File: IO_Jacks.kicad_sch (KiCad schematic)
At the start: 45 parts, among them J10 3085_MiniJack_Thonk_Vert, J11 3085_MiniJack_Thonk_Vert, J12 3085_MiniJack_Thonk_Vert, J13 3085_MiniJack_Thonk_Vert, J5 CV_OFFSET, J6 3085_MiniJack_Thonk_Vert, J7 3085_MiniJack_Thonk_Vert, J8 3085_MiniJack_Thonk_Vert, J9 3085_MiniJack_Thonk_Vert, U5 4014_Voltage_Reference_5V_SOT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

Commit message: some more routing
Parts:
- removed TP21: DAC_VOUT0, Shulltronics_Generics:TestPoint_Pad_D2.0mm, symbol Shulltronics_Sch_Symbols:TestPoint
- removed TP25: DAC_VOUT2, Shulltronics_Generics:TestPoint_Pad_D2.0mm, symbol Shulltronics_Sch_Symbols:TestPoint
- removed TP26: DAC_VOUT3, Shulltronics_Generics:TestPoint_Pad_D2.0mm, symbol Shulltronics_Sch_Symbols:TestPoint
- removed TP29: TRIG1, Shulltronics_Generics:TestPoint_Pad_D2.0mm, symbol Shulltronics_Sch_Symbols:TestPoint
- removed TP30: TRIG2, Shulltronics_Generics:TestPoint_Pad_D2.0mm, symbol Shulltronics_Sch_Symbols:TestPoint
- removed TP31: TRIG3, Shulltronics_Generics:TestPoint_Pad_D2.0mm, symbol Shulltronics_Sch_Symbols:TestPoint
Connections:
- net TRIG2: now also U8.12 (4IN+); no longer U8.10 (3IN+)
- net TRIG2_FB: now also U8.13 (4IN-), U8.14 (4OUT); no longer U8.8 (3OUT), U8.9 (3IN-)
- net TRIG3: now also U8.10 (3IN+); no longer U8.12 (4IN+)
- net TRIG3_FB: now also U8.8 (3OUT), U8.9 (3IN-); no longer U8.13 (4IN-), U8.14 (4OUT)
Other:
- moved on the sheet: U8C, U8D

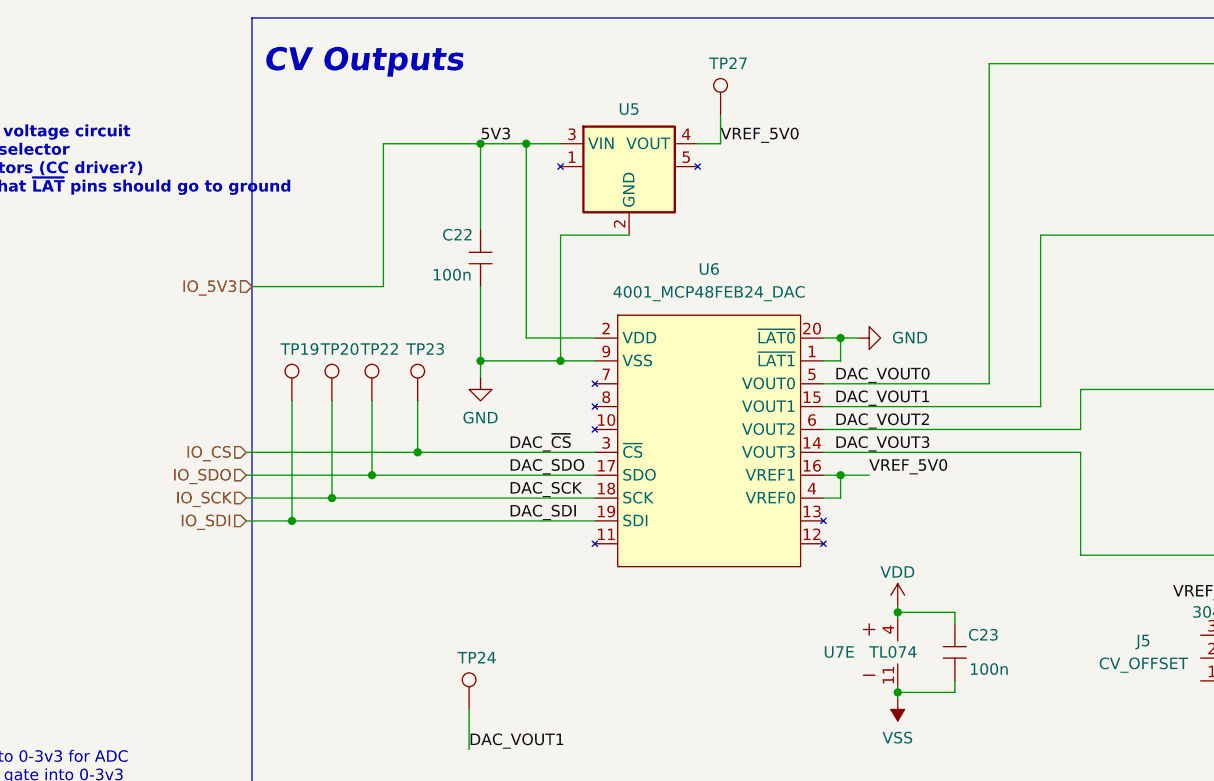
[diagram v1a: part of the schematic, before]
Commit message: Added a few 0 ohm options, finished routing, ordered board!
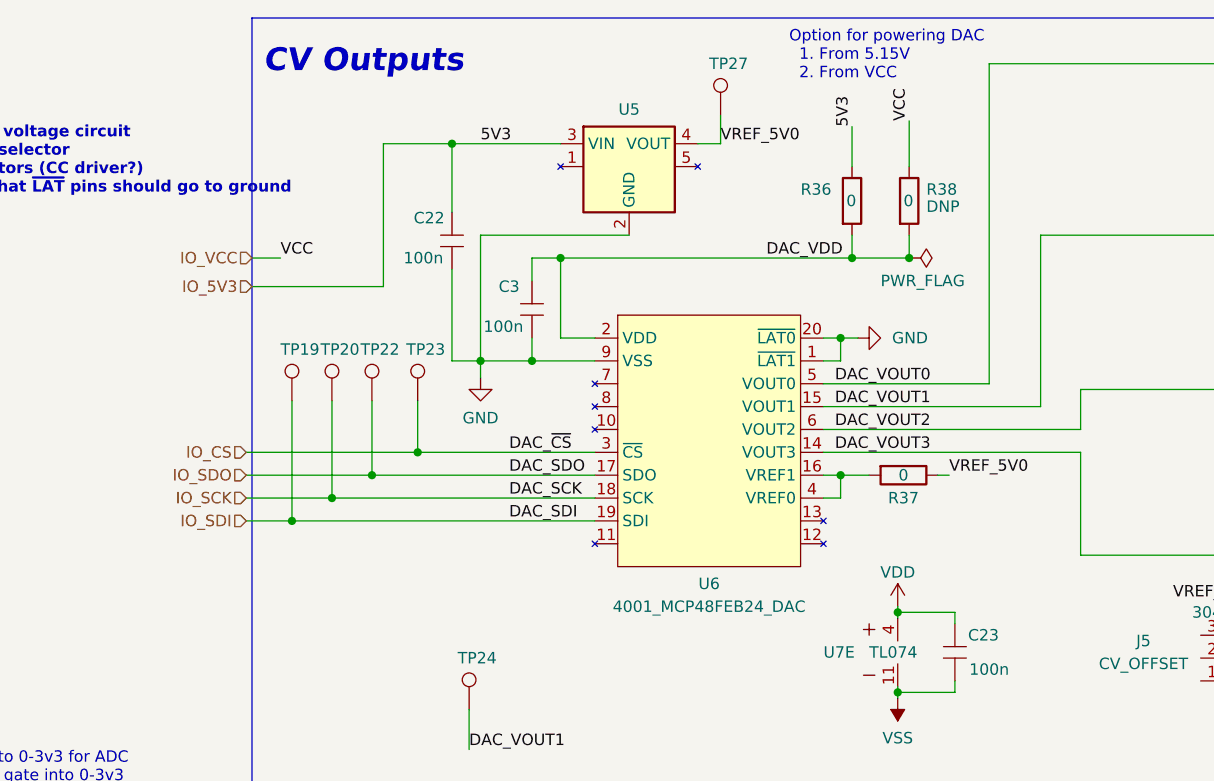
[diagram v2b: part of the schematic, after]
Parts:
- added C3: 3089_Capacitor_100n_16V_SMD, Shulltronics_Generics:C_0402_HandSolder, symbol Shulltronics_Passives:3089_Capacitor_100n_16V_0402
- added R36: 4021_Resistor_SMD_Jumper, Shulltronics_Generics:RES-0402, symbol Shulltronics_Passives:4021_Resistor_SMD_Jumper
- added R37: JMP, Shulltronics_Generics:RES-0402, symbol Shulltronics_Passives:4021_Resistor_SMD_Jumper
- added R38: DNP, Shulltronics_Generics:RES-0402, symbol Shulltronics_Passives:4021_Resistor_SMD_Jumper
- J5: footprint Shulltronics_Connectors:3046_Header_3pos_2.54mm -> Shulltronics_Generics:SMD_SolderJumper-3
- TP19: value DAC_SDI -> SDI
- TP20: value DAC_SCK -> SCK
- TP22: value DAC_SDO -> SDO
- TP23: value DAC_~{CS} -> ~{CS}
- TP24: value DAC_VOUT1 -> DAC1
- TP27: value VREF_5V0 -> 5V0
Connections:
- net GND: now also C3.1
- net IO_5V3: now also R36.1; no longer U6.2 (VDD)
- net VREF_5V0: now also R37.1; no longer U6.16 (VREF1), U6.4 (VREF0)
- new net: R37.2, U6.16 (VREF1), U6.4 (VREF0)
- new net DAC_VDD: C3.2, R36.2, R38.2, U6.2 (VDD)
- new net IO_VCC: R38.1
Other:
- note added: "Option for powering DAC 1. From 5.15V 2. From VCC"
- moved on the sheet: C22

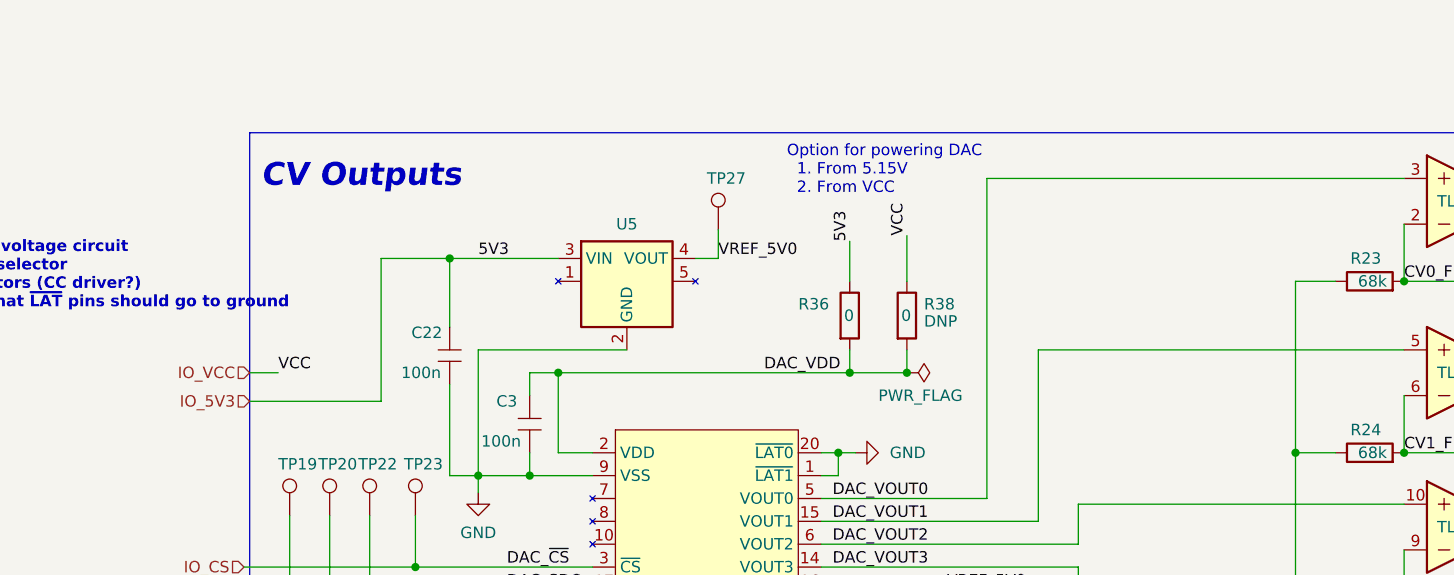
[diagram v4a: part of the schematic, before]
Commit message: Updated a few things from testing voltage regulators
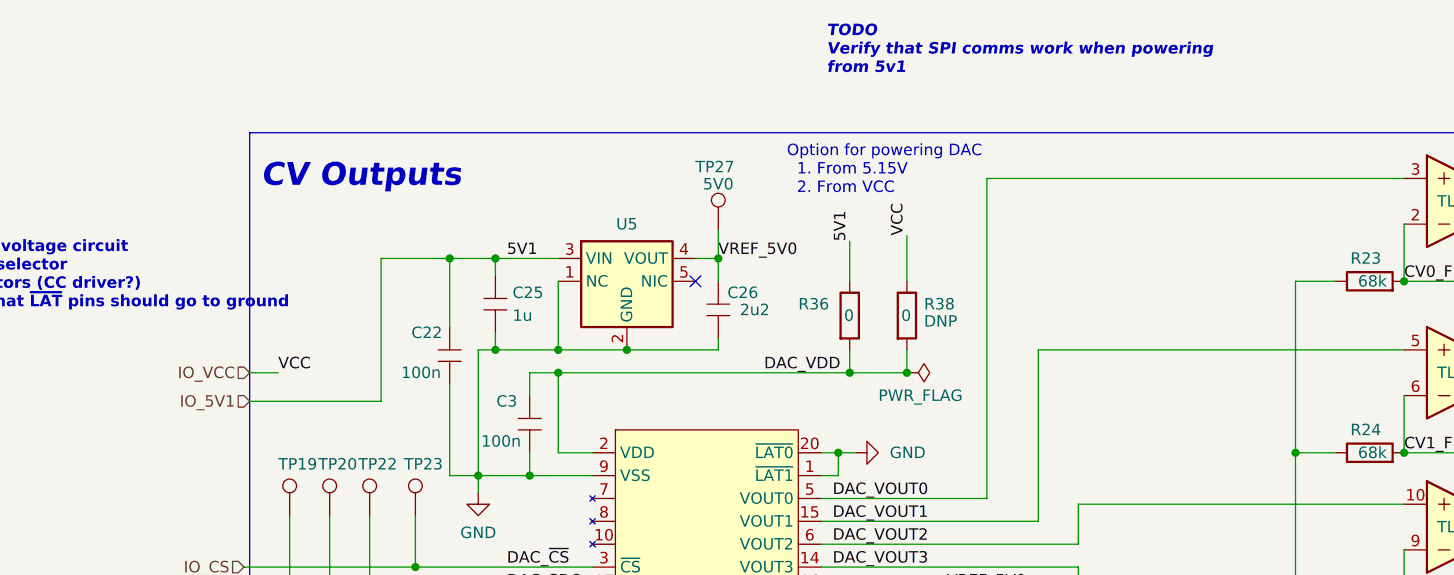
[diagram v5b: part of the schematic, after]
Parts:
- added C25: 4013_Capacitor_1u_16V_0402, Shulltronics_Generics:C_0402_HandSolder, symbol Shulltronics_Passives:4013_Capacitor_1u_16V_0402
- added C26: 4035_Capacitor_2u2_25V_0402, Shulltronics_Generics:C_0402_HandSolder, symbol Shulltronics_Passives:4035_Capacitor_2u2_25V_0402
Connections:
- net GND: now also U5.1 (NC), C25.1, C26.2
- net VREF_5V0: now also C26.1
- net IO_5V3 renamed IO_5V1
- net IO_5V1: now also C25.2
- no-connect marks 8 -> 9
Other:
- note added: "TODO Verify that SPI comms work when powering from 5v1"
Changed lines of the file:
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@@
   (junction (at 140.335 163.83) (diameter 0) (color 0 0 0 0)
   )
+  (junction (at 99.06 38.1) (diameter 0) (color 0 0 0 0)
+  )
   (junction (at 193.04 30.48) (diameter 0) (color 0 0 0 0)
   )
@@
   (junction (at 208.28 40.64) (diameter 0) (color 0 0 0 0)
   )
+  (junction (at 92.075 27.94) (diameter 0) (color 0 0 0 0)
+  )
   (junction (at 137.795 40.64) (diameter 0) (color 0 0 0 0)
   )
@@
   (junction (at 99.06 40.64) (diameter 0) (color 0 0 0 0)
   )
+  (junction (at 116.84 27.94) (diameter 0) (color 0 0 0 0)
+  )
   (junction (at 136.525 88.9) (diameter 0) (color 0 0 0 0)
   )
@@
   (junction (at 173.99 112.395) (diameter 0) (color 0 0 0 0)
   )
+  (junction (at 92.075 38.1) (diameter 0) (color 0 0 0 0)
+  )
   (junction (at 158.75 153.67) (diameter 0) (color 0 0 0 0)
   )
@@
   (junction (at 173.355 153.67) (diameter 0) (color 0 0 0 0)
   )
+  (junction (at 106.68 38.1) (diameter 0) (color 0 0 0 0)
+  )
   (junction (at 212.725 126.365) (diameter 0) (color 0 0 0 0)
   )
@@
   (junction (at 238.125 121.285) (diameter 0) (color 0 0 0 0)
   )
+  (no_connect (at 114.3 30.48))
   (no_connect (at 215.9 121.285))
   (no_connect (at 215.9 135.255))
@@
     (stroke (width 0) (type default) (color 0 0 0 0))
   )
+  (wire (pts (xy 92.075 27.94) (xy 92.075 29.845))
+    (stroke (width 0) (type default) (color 0 0 0 0))
+  )
   (wire (pts (xy 130.81 112.395) (xy 130.81 155.575))
     (stroke (width 0) (type default) (color 0 0 0 0))
@@
     (stroke (width 0) (type default) (color 0 0 0 0))
   )
+  (wire (pts (xy 92.075 27.94) (xy 99.06 27.94))
+    (stroke (width 0) (type default) (color 0 0 0 0))
+  )
   (wire (pts (xy 156.845 55.245) (xy 156.845 59.69))
     (stroke (width 0) (type default) (color 0 0 0 0))
@@
     (stroke (width 0) (type default) (color 0 0 0 0))
   )
+  (wire (pts (xy 116.84 36.83) (xy 116.84 38.1))
+    (stroke (width 0) (type default) (color 0 0 0 0))
+  )
   (wire (pts (xy 158.75 153.67) (xy 163.83 153.67))
     (stroke (width 0) (type default) (color 0 0 0 0))
@@
     (stroke (width 0) (type default) (color 0 0 0 0))
   )
+  (wire (pts (xy 116.84 27.94) (xy 116.84 30.48))
+    (stroke (width 0) (type default) (color 0 0 0 0))
+  )
   (wire (pts (xy 180.975 66.675) (xy 185.42 66.675))
     (stroke (width 0) (type default) (color 0 0 0 0))
@@
     (stroke (width 0) (type default) (color 0 0 0 0))
   )
-  (wire (pts (xy 90.17 38.1) (xy 106.68 38.1))
+  (wire (pts (xy 90.17 38.1) (xy 92.075 38.1))
     (stroke (width 0) (type default) (color 0 0 0 0))
   )
@@
     (stroke (width 0) (type default) (color 0 0 0 0))
   )
-  (wire (pts (xy 86.995 27.94) (xy 99.06 27.94))
+  (wire (pts (xy 86.995 27.94) (xy 92.075 27.94))
     (stroke (width 0) (type default) (color 0 0 0 0))
   )
@@
     (stroke (width 0) (type default) (color 0 0 0 0))
   )
+  (wire (pts (xy 99.06 38.1) (xy 106.68 38.1))
+    (stroke (width 0) (type default) (color 0 0 0 0))
+  )
   (wire (pts (xy 114.3 27.94) (xy 116.84 27.94))
     (stroke (width 0) (type default) (color 0 0 0 0))
@@
     (stroke (width 0) (type default) (color 0 0 0 0))
   )
+  (wire (pts (xy 116.84 38.1) (xy 106.68 38.1))
+    (stroke (width 0) (type default) (color 0 0 0 0))
+  )
   (wire (pts (xy 175.895 78.74) (xy 175.895 82.55))
     (stroke (width 0) (type default) (color 0 0 0 0))
@@
     (stroke (width 0) (type default) (color 0 0 0 0))
   )
+  (wire (pts (xy 92.075 36.195) (xy 92.075 38.1))
+    (stroke (width 0) (type default) (color 0 0 0 0))
+  )
   (polyline (pts (xy 64.77 99.06) (xy 229.235 99.06))
     (stroke (width 0) (type default) (color 0 0 0 0))
@@
     (stroke (width 0) (type default) (color 0 0 0 0))
   )
+  (wire (pts (xy 99.06 30.48) (xy 99.06 38.1))
+    (stroke (width 0) (type default) (color 0 0 0 0))
+  )
   (wire (pts (xy 130.175 49.53) (xy 132.08 49.53))
     (stroke (width 0) (type default) (color 0 0 0 0))
@@
   )
   (wire (pts (xy 131.445 26.035) (xy 131.445 30.48))
+    (stroke (width 0) (type default) (color 0 0 0 0))
+  )
+  (wire (pts (xy 92.075 38.1) (xy 99.06 38.1))
     (stroke (width 0) (type default) (color 0 0 0 0))
   )
@@
     (effects (font (size 1.27 1.27)) (justify left bottom))
   )
+  (text "TODO\nVerify that SPI comms work when powering\nfrom 5v1"
+    (at 128.905 7.62 0)
+    (effects (font (size 1.27 1.27) (thickness 0.254) bold italic) (justify left bottom))
+  )
   (text "Option for powering DAC\n  1. From 5.15V\n  2. From VCC"
     (at 124.46 20.955 0)
@@
     (effects (font (size 1.27 1.27)) (justify left bottom))
   )
-  (label "5V3" (at 90.17 27.94 0)
+  (label "5V1" (at 93.345 27.94 0)
     (effects (font (size 1.27 1.27)) (justify left bottom))
   )
@@
     (effects (font (size 1.27 1.27)) (justify left bottom))
   )
-  (label "5V3" (at 131.445 26.035 90)
+  (label "5V1" (at 131.445 26.035 90)
     (effects (font (size 1.27 1.27)) (justify left bottom))
   )
@@
     (effects (font (size 1.27 1.27)) (justify right))
   )
-  (hierarchical_label "IO_5V3" (shape input) (at 64.77 43.815 180)
+  (hierarchical_label "IO_5V1" (shape input) (at 64.77 43.815 180)
     (effects (font (size 1.27 1.27)) (justify right))
   )
@@
     (pin "1")
   )
+  (symbol (lib_id "Shulltronics_Passives:4013_Capacitor_1u_16V_0402") (at 92.075 32.385 90) (unit 1)
+    (in_bom yes) (on_board yes) (fields_autoplaced)
+    (property "Reference" "C25" (id 0) (at 93.98 31.7499 90)
+      (effects (font (size 1.27 1.27)) (justify right))
+    )
+    (property "Value" "4013_Capacitor_1u_16V_0402" (id 1) (at 99.695 32.385 0)
+      (effects (font (size 1.27 1.27)) hide)
+    )
+    (property "Footprint" "Shulltronics_Generics:C_0402_HandSolder" (id 2) (at 97.155 32.385 0)
+      (effects (font (size 1.27 1.27)) hide)
+    )
+    (property "Datasheet" "https://media.digikey.com/pdf/Data%20Sheets/Samsung%20PDFs/CL05A104KA5NNNC.pdf" (id 3) (at 102.235 32.385 0)
+      (effects (font (size 1.27 1.27)) hide)
+    )
+    (property "SPN" "4013" (id 4) (at 94.615 32.385 0)
+      (effects (font (size 1.27 1.27)) hide)
+    )
+    (property "Val" "1u" (id 5) (at 93.98 34.2899 90)
+      (effects (font (size 1.27 1.27)) (justify right))
+    )
+    (pin "1")
+    (pin "2")
+  )
   (symbol (lib_id "Shulltronics_ICs:3099_TL074CPW_SMD") (at 199.39 76.2 0) (unit 4)
     (in_bom yes) (on_board yes)
@@
     (pin "TN")
   )
+  (symbol (lib_id "Shulltronics_Passives:4035_Capacitor_2u2_25V_0402") (at 116.84 34.29 270) (unit 1)
+    (in_bom yes) (on_board yes)
+    (property "Reference" "C26" (id 0) (at 121.285 31.75 90)
+      (effects (font (size 1.27 1.27)) (justify right))
+    )
+    (property "Value" "4035_Capacitor_2u2_25V_0402" (id 1) (at 109.22 34.29 0)
+      (effects (font (size 1.27 1.27)) hide)
+    )
+    (property "Footprint" "Shulltronics_Generics:C_0402_HandSolder" (id 2) (at 111.76 34.29 0)
+      (effects (font (size 1.27 1.27)) hide)
+    )
+    (property "Datasheet" "https://media.digikey.com/pdf/Data%20Sheets/Samsung%20PDFs/CL_Series_MLCC_ds.pdf" (id 3) (at 106.68 34.29 0)
+      (effects (font (size 1.27 1.27)) hide)
+    )
+    (property "SPN" "4035" (id 4) (at 114.3 34.29 0)
+      (effects (font (size 1.27 1.27)) hide)
+    )
+    (property "Val" "2u2" (id 5) (at 122.555 33.655 90)
+      (effects (font (size 1.27 1.27)) (justify right))
+    )
+    (pin "1")
+    (pin "2")
+  )
   (symbol (lib_id "Shulltronics_Sch_Symbols:TestPoint") (at 83.185 56.515 0) (unit 1)
     (in_bom yes) (on_board yes)
@@
   (symbol (lib_id "Shulltronics_Sch_Symbols:TestPoint") (at 116.84 24.765 0) (unit 1)
     (in_bom yes) (on_board yes)
-    (property "Reference" "TP27" (id 0) (at 115.57 19.05 0)
-      (effects (font (size 1.27 1.27)) (justify left))
-    )
-    (property "Value" "5V0" (id 1) (at 116.84 19.685 0)
-      (effects (font (size 1.27 1.27)) hide)
-    )
+    (property "Reference" "TP27" (id 0) (at 114.3 17.78 0)
+      (effects (font (size 1.27 1.27)) (justify left))
+    )
+    (property "Value" "5V0" (id 1) (at 116.84 19.685 0))
     (property "Footprint" "Shulltronics_Generics:TestPoint_Pad_D2.0mm" (id 2) (at 121.92 24.765 0)
       (effects (font (size 1.27 1.27)) hide)
